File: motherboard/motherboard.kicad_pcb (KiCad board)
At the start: 2 copper layers, 42.9 x 71.7 mm, 28 parts, among them J1 Conn_01x12_MountingPin, J2 Conn_01x12_MountingPin, J3 Conn_01x12_MountingPin, J4 Conn_01x12_MountingPin, J5 Conn_01x12_MountingPin, J6 Conn_01x12_MountingPin, J7 USB_C_Receptacle_USB2.0, SW1 RESET, SW2 BOOT, U1 SRV05-4, U2 M3406-ADJ, U3 ESP32-S3-WROOM-1

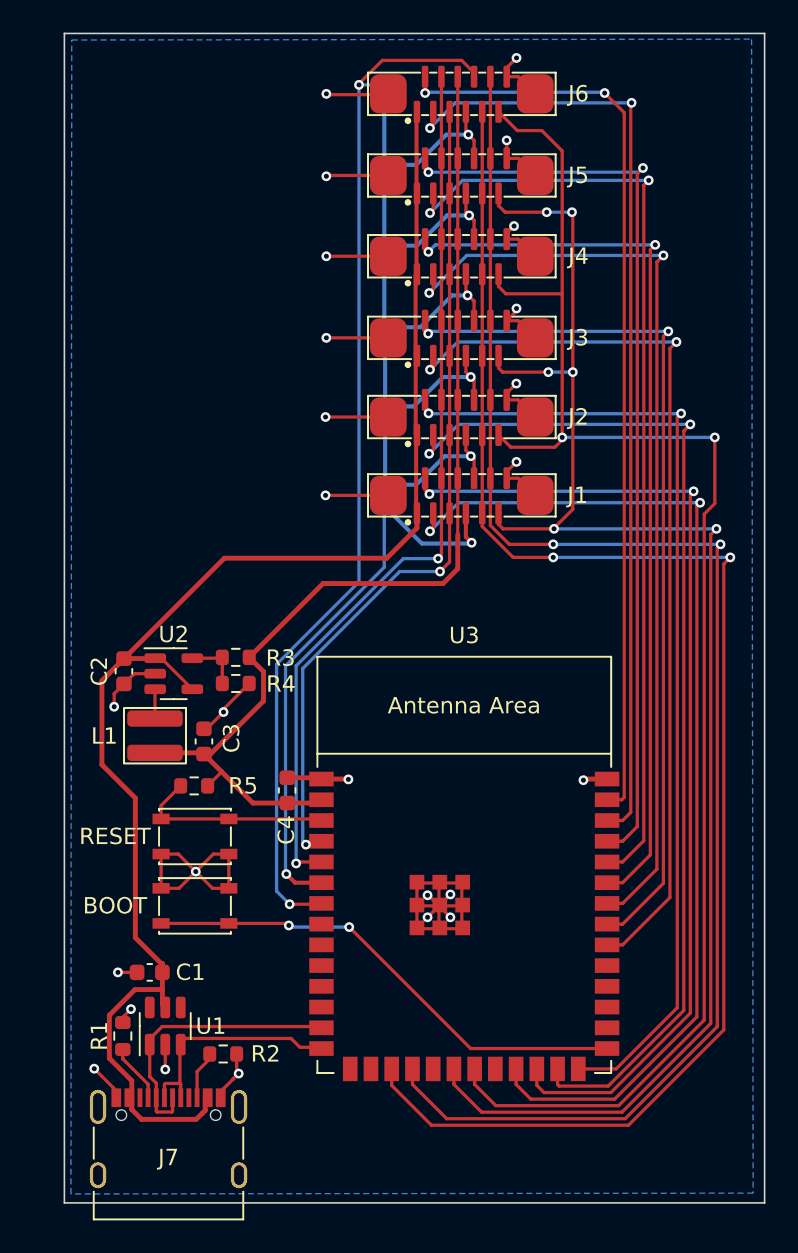
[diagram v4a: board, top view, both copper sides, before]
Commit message: Quick relayout of motherboard - rotate ESP32, move supporting parts to bottom edge, reroute traces
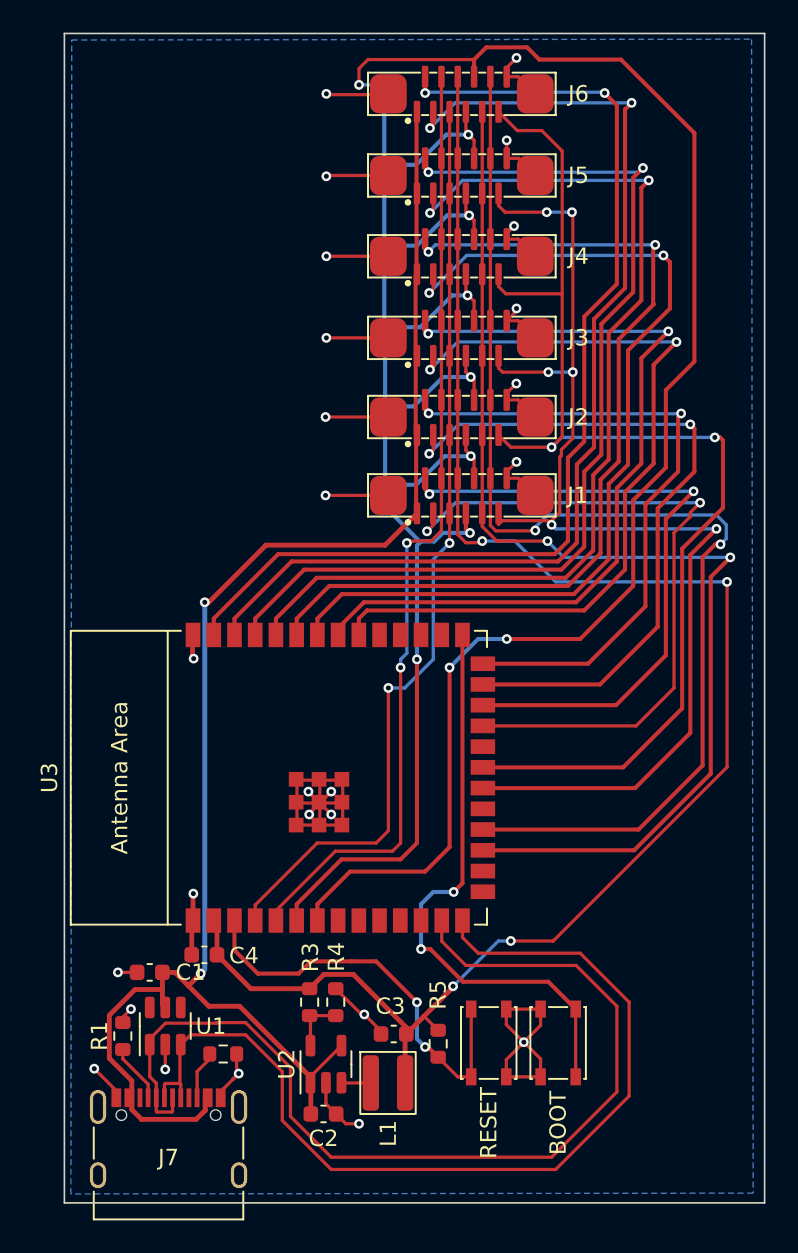
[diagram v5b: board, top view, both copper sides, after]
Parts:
- moved C2 29.8 mm to (44.8, 112.1), turned to 0 degrees
- moved U2 25.7 mm to (44.9, 109.0), turned to 90 degrees
- moved L1 25.6 mm to (48.7, 110.2), turned to 0 degrees
- moved SW2 23.8 mm to (59.1, 107.8), turned to 90 degrees
- moved SW1 22.0 mm to (54.9, 107.8), turned to -90 degrees
- moved R5 21.8 mm to (51.8, 107.8), turned to -90 degrees
- moved R3 21.6 mm to (43.9, 105.2), turned to 90 degrees
- moved C3 21.4 mm to (49.1, 107.2), turned to 180 degrees
- moved R4 20.5 mm to (45.5, 105.2), turned to -90 degrees
- moved U3 11.8 mm to (45.0, 91.5), turned to 90 degrees
- moved C4 11.3 mm to (37.5, 102.3), turned to 180 degrees
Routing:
- net /D+: track 13.8 -> 58.5 mm
- net /D-: track 16.9 -> 61.2 mm
- net /VDD: track 65.9 -> 104.7 mm, vias 0 -> 4
- net /MISO6: track 64.5 -> 91.1 mm, vias 2 -> 3
- net /SCLK: track 95.3 -> 71.0 mm
- net /POL1: track 94.9 -> 72.1 mm
- net /SDA1: track 62.0 -> 40.6 mm
- net /POL2: track 94.9 -> 73.7 mm
- net /SCL1: track 64.5 -> 43.4 mm
- net /SCL2: track 64.7 -> 43.6 mm
- net /SS: track 94.5 -> 73.5 mm
- net /SDA2: track 60.5 -> 40.5 mm
- net Net-(U3-EN): track 12.4 -> 25.6 mm, vias 0 -> 2
- net /SDA6: track 56.8 -> 65.7 mm
- net /VIN: track 91.5 -> 99.3 mm, vias 0 -> 2
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
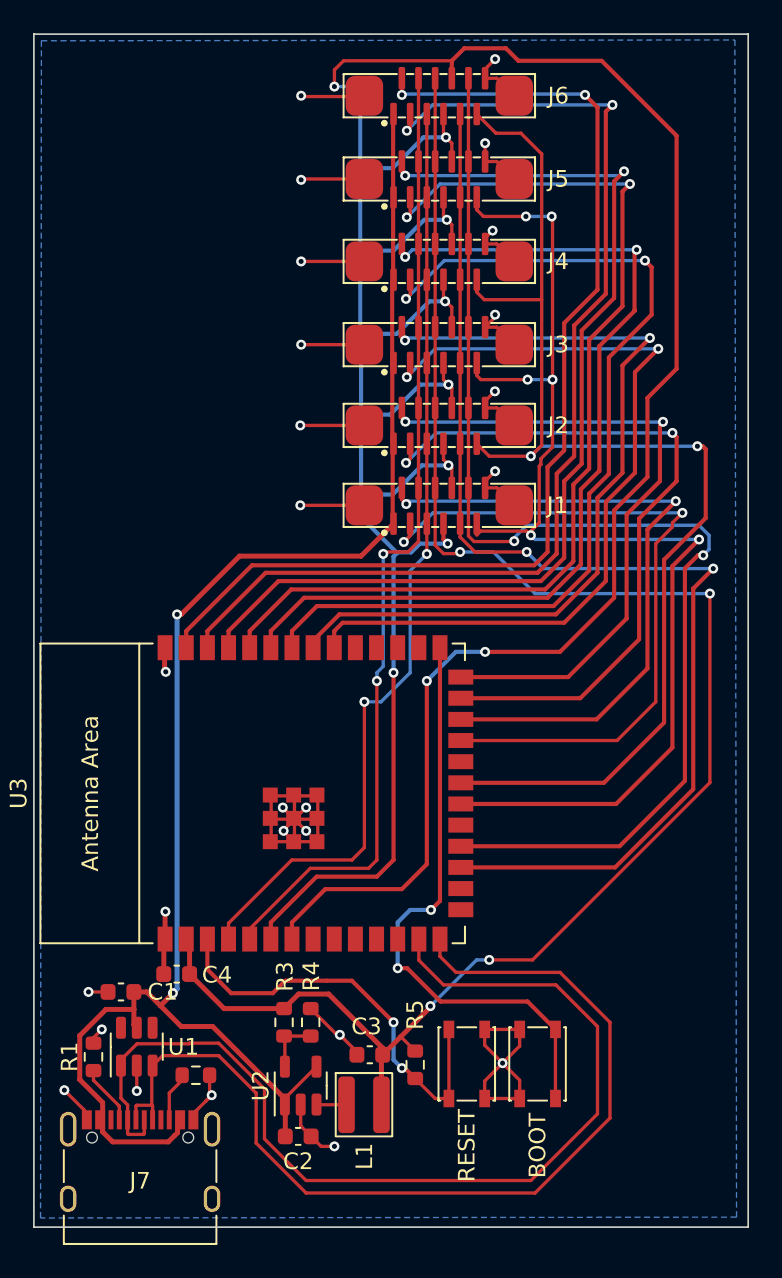
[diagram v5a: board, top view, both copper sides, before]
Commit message: motherboard low pass filter
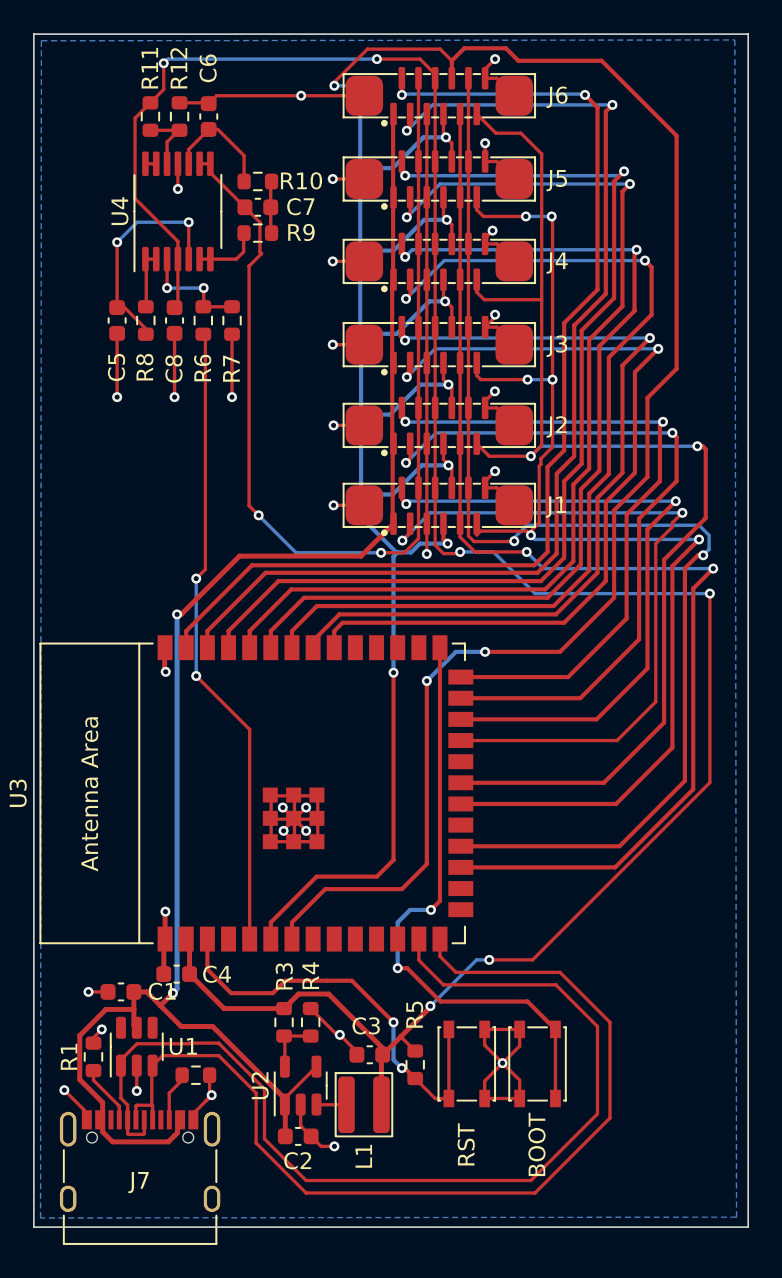
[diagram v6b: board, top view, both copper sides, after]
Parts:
- added C5: 0.01µF, Capacitor_SMD:C_0603_1608Metric, F.Cu at (33.9, 63.1)
- added C6: 0.01µF, Capacitor_SMD:C_0603_1608Metric, F.Cu at (39.4, 50.9)
- added C7: 0.047µF, Capacitor_SMD:C_0603_1608Metric, F.Cu at (42.4, 56.3)
- added C8: 0.01µF, Capacitor_SMD:C_0603_1608Metric, F.Cu at (37.4, 63.1)
- added R10: 2.74K, Resistor_SMD:R_0603_1608Metric, F.Cu at (42.4, 54.8)
- added R11: 100K, Resistor_SMD:R_0603_1608Metric, F.Cu at (35.9, 50.9)
- added R12: 100K, Resistor_SMD:R_0603_1608Metric, F.Cu at (37.6, 50.9)
- added R6: 12.4K, Resistor_SMD:R_0603_1608Metric, F.Cu at (39.1, 63.1)
- added R7: 6.19K, Resistor_SMD:R_0603_1608Metric, F.Cu at (40.8, 63.1)
- added R8: 4.02K, Resistor_SMD:R_0603_1608Metric, F.Cu at (35.6, 63.1)
- added R9: 1.21K, Resistor_SMD:R_0603_1608Metric, F.Cu at (42.4, 57.9)
- added U4: LM324, Package_SO:TSSOP-14_4.4x5mm_P0.65mm, F.Cu at (37.5, 56.5)
- SW1: value RESET -> RST
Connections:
- J1 pad 5: /IN- -> GND
- J2 pad 5: /IN- -> GND
- J3 pad 5: /IN- -> GND
- J4 pad 5: /IN- -> GND
- J5 pad 5: /IN- -> GND
- J6 pad 5: /IN- -> GND
- U3 pad 4: /IN- -> /microcontroller/GPIO4
- U3 pad 5: /IN+ -> /PWM_OUT
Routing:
- net /IN-: track 57.2 -> 0.00 mm, vias 2 -> 0
- net /PWM_OUT: track 0.00 -> 38.0 mm, vias 0 -> 2
- net GND: track 100.3 -> 137.5 mm, vias 26 -> 31
- net /VDD: track 104.7 -> 138.1 mm, vias 4 -> 6
- net Net-(U4B-+): track 0.00 -> 13.5 mm, vias 0 -> 2
- net Net-(U4C-+): track 0.00 -> 6.89 mm
- net Net-(U4A-+): track 0.00 -> 6.80 mm, vias 0 -> 2
- net Net-(U4D-+): track 0.00 -> 4.00 mm
- net Net-(U4B--): track 0.00 -> 3.97 mm
- net Net-(U4A--): track 0.00 -> 3.48 mm
- net /IN+: track 58.8 -> 62.1 mm
- net Net-(C7-Pad1): track 0.00 -> 3.14 mm
- net Net-(U4D--): track 0.00 -> 0.65 mm

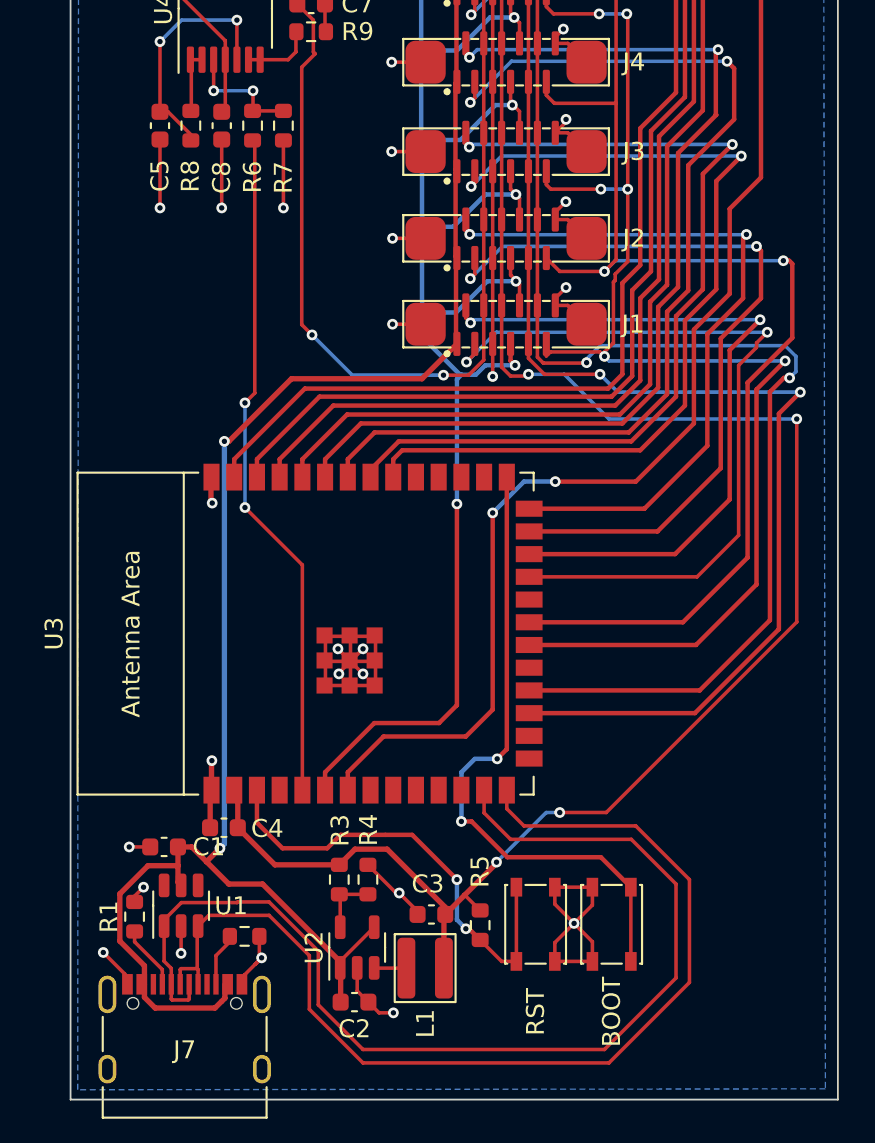
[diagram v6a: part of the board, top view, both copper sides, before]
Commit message: motherboard add test points
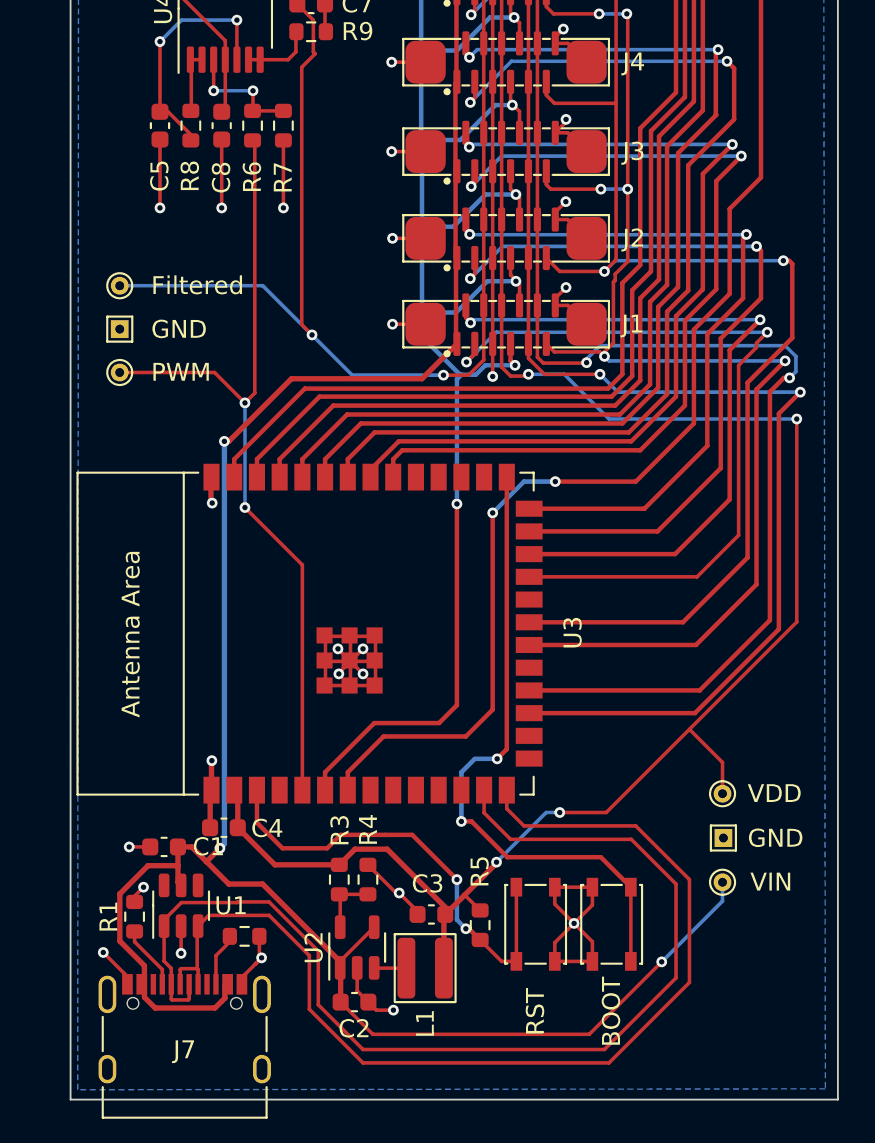
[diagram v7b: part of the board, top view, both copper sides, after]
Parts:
- added TP1: PWM, TestPoint:TestPoint_THTPad_D1.0mm_Drill0.5mm, F.Cu at (31.6, 76.9)
- added TP2: Filtered, TestPoint:TestPoint_THTPad_D1.0mm_Drill0.5mm, F.Cu at (31.6, 72.0)
- added TP3: GND, TestPoint:TestPoint_THTPad_1.0x1.0mm_Drill0.5mm, F.Cu at (31.6, 74.5)
- added TP4: VIN, TestPoint:TestPoint_THTPad_D1.0mm_Drill0.5mm, F.Cu at (65.3, 105.4)
- added TP5: GND, TestPoint:TestPoint_THTPad_1.0x1.0mm_Drill0.5mm, F.Cu at (65.4, 102.9)
- added TP6: VDD, TestPoint:TestPoint_THTPad_D1.0mm_Drill0.5mm, F.Cu at (65.3, 100.5)
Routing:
- net /VIN: track 99.3 -> 125.5 mm, vias 2 -> 3
- net /IN+: track 62.1 -> 74.0 mm
- net /PWM_OUT: track 38.0 -> 45.7 mm
- net /VDD: track 138.1 -> 142.4 mm
- net /POL1: track 72.1 -> 71.5 mm

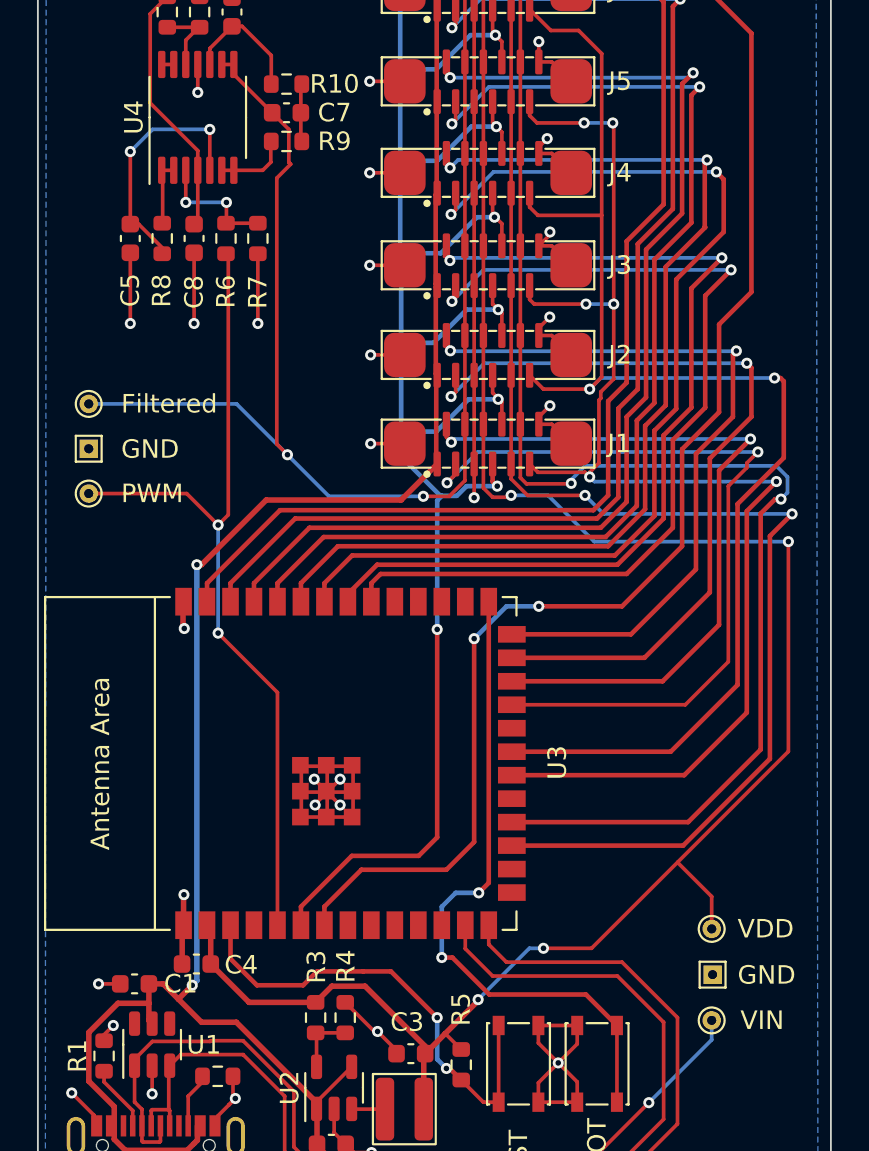
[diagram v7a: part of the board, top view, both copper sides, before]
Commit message: add 1st order low pass filter, with solder jumper
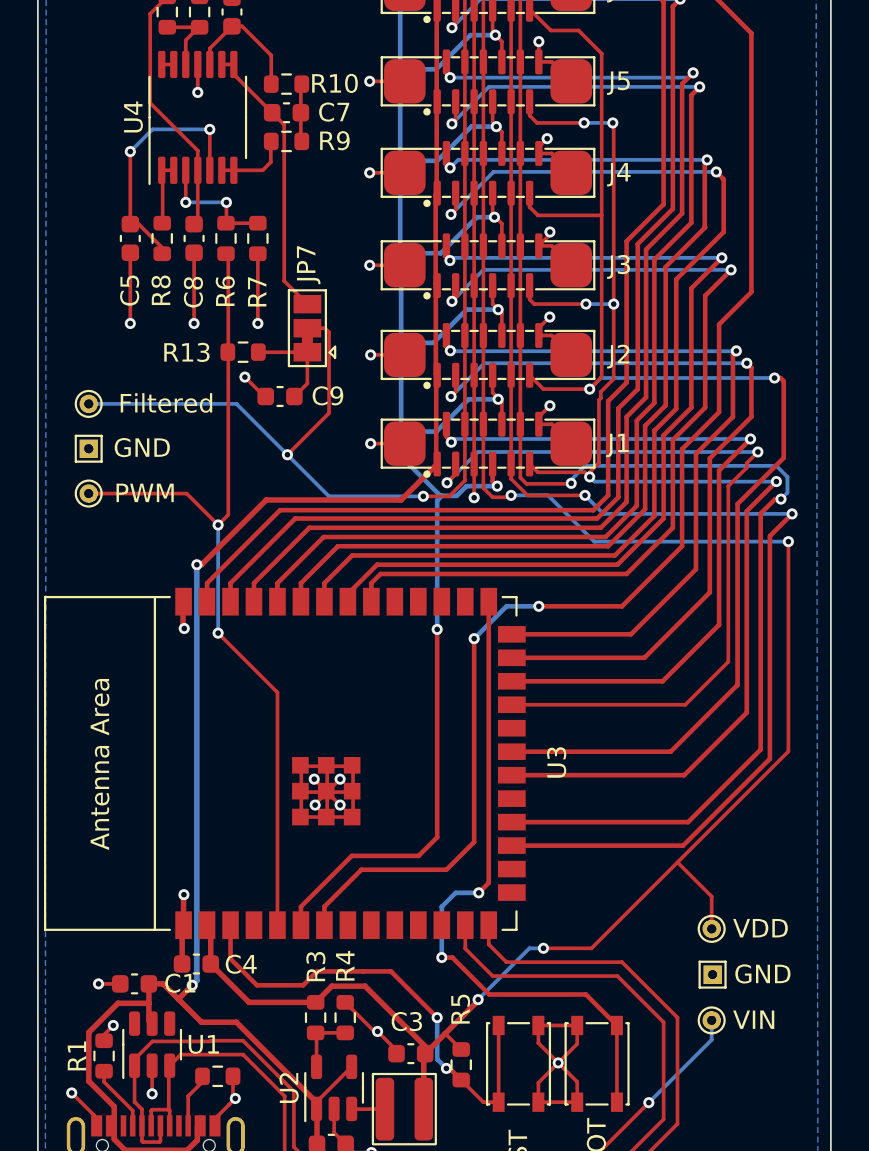
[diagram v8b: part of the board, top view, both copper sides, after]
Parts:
- added C9: 0.1µF, Capacitor_SMD:C_0603_1608Metric, F.Cu at (42.0, 71.7)
- added JP7: SolderJumper_3_Bridged12, Jumper:SolderJumper-3_P1.3mm_Bridged12_Pad1.0x1.5mm, F.Cu at (43.5, 68.0)
- added R13: 390, Resistor_SMD:R_0603_1608Metric, F.Cu at (40.0, 69.2)
- TP1: value PWM -> TestPoint
- TP2: value Filtered -> TestPoint
- TP3, TP5: value GND -> TestPoint
- TP4: value VIN -> TestPoint
- TP6: value VDD -> TestPoint
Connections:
- C7 pad 2: /IN+ -> Net-(JP7-B)
- U4 pad 8: /IN+ -> Net-(JP7-B)
- U4 pad 9: /IN+ -> Net-(JP7-B)
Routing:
- net Net-(JP7-B): track 0.00 -> 15.3 mm
- net /IN+: track 74.0 -> 59.2 mm
- net Net-(JP7-A): track 0.00 -> 5.34 mm
- net GND: track 137.4 -> 139.0 mm, vias 31 -> 32
